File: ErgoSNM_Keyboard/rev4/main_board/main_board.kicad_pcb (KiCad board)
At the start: 2 copper layers, 116 parts, among them J1 Conn_MouseSensor, J2 Conn_CoreBoard, J3 Conn_MouseSensor, J4 Conn_Batt, J5 Conn_Batt, J6 Conn_CoreBoard, SW1 SW_DPDT_x2, SW2 RESET, SW3 RESET, SW4 SW_DPDT_x2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

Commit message: feat: update main board layout
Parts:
- removed C1, C2, C5, C6, C7, C8: 22uF, Capacitor_SMD:C_0805_2012Metric
- removed C10: 1uF, Capacitor_SMD:C_0603_1608Metric
- removed C11, C12: 4.7uF, Capacitor_SMD:C_0603_1608Metric
- removed C3, C4: 2.2uF, Capacitor_SMD:C_0603_1608Metric
- removed C9: 100nF, Capacitor_SMD:C_0603_1608Metric
- removed J4, J5: Conn_Batt, Connector_JST:JST_PH_S2B-PH-SM4-TB_1x02-1MP_P2.00mm_Horizontal
- removed L1: 1.5uH, Inductor_SMD:L_Changjiang_FNR252012S
- removed LD1, LD2: RED, LED_SMD:LED_0603_1608Metric
- removed R2: 1M, Resistor_SMD:R_0603_1608Metric
- removed R3: 180k, Resistor_SMD:R_0603_1608Metric
- removed R4, R5, R7: 10k, Resistor_SMD:R_0603_1608Metric
- removed R6: 2k, Resistor_SMD:R_0603_1608Metric
- removed SB1: Batt Switch Bypass, Jumper:SolderJumper-2_P1.3mm_Open_TrianglePad1.0x1.5mm
- removed SB2: Charger Select, Jumper:SolderJumper-3_P2.0mm_Open_TrianglePad1.0x1.5mm_NumberLabels
- removed SB3: Vsrc Select, Jumper:SolderJumper-3_P2.0mm_Open_TrianglePad1.0x1.5mm_NumberLabels
- removed SB4: Power Save, Jumper:SolderJumper-3_P2.0mm_Open_TrianglePad1.0x1.5mm_NumberLabels
- removed SB5: Charge Boost, Jumper:SolderJumper-2_P1.3mm_Open_TrianglePad1.0x1.5mm
- removed SW1, SW4: SW_DPDT_x2, ErgoSNM_Keyboard:MSKT-22D14-T
- removed TRRS1, TRRS2: PJ-393_TRRS_8P, ErgoSNM_Keyboard:PJ-393 8P TRRS
- removed U1: TPS63020, Package_SON:VSON-14-1EP_3x4.45mm_P0.65mm_EP1.6x4.2mm_ThermalVias
- removed U2: BQ24075RGT, Package_DFN_QFN:VQFN-16-1EP_3x3mm_P0.5mm_EP1.6x1.6mm
- H1, H2, H3, H4, H5, H6, R1: moved to B.Cu
- moved R1 148.6 mm to (96.0, 49.0), turned to -90 degrees
- moved J2 102.0 mm to (117.8, 46.4), turned to 0 degrees
- moved J6 102.0 mm to (117.8, 46.4), turned to 180 degrees
- moved SW2 4.79 mm to (101.5, 49.0)
- moved SW3 4.79 mm to (101.5, 49.0)
- moved J1 0.42 mm to (194.0, 133.1)
- moved J3 0.42 mm to (194.0, 133.1)
- turned H1 to 180 degrees
- turned H2 to 180 degrees
- turned H3 to 180 degrees
- turned H4 to 180 degrees
- turned H5 to 180 degrees
- turned H6 to 180 degrees
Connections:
- J2 pad 1: VBATT_{A} -> GND
- J2 pad 10: SCLK -> COL_1
- J2 pad 11: MOSI -> COL_0
- J2 pad 12: MISO -> ROW_4
- J2 pad 13: nCS -> ROW_3
- J2 pad 14: ROW_0 -> unconnected-(J2-Pin_14-Pad14)
- J2 pad 15: ROW_1 -> ROW_2
- J2 pad 16: ROW_2 -> ROW_1
- J2 pad 17: GND -> ROW_0
- J2 pad 18: ROW_3 -> nCS
- J2 pad 19: ROW_4 -> MISO
- J2 pad 2: VBUS -> unconnected-(J2-Pin_2-Pad2)
- J2 pad 20: COL_0 -> MOSI
- J2 pad 21: COL_1 -> SCLK
- J2 pad 22: COL_2 -> MOTION
- J2 pad 23: COL_3 -> unconnected-(J2-Pin_23-Pad23)
- J2 pad 24: COL_4 -> unconnected-(J2-Pin_24-Pad24)
- J2 pad 25: COL_5 -> GND
- J2 pad 26: GND -> RESET
- J2 pad 27: IO_0 -> VDD
- J2 pad 28: IO_1 -> VDD
- J2 pad 29: IO_2 -> unconnected-(J2-Pin_29-Pad29)
- J2 pad 3: VDD -> unconnected-(J2-Pin_3-Pad3)
- J2 pad 30: GND -> unconnected-(J2-Pin_30-Pad30)
- J2 pad 4: VDD -> IO_0
- J2 pad 5: RESET -> GND
- J2 pad 6: GND -> COL_5
- J2 pad 7: TX -> COL_4
- J2 pad 8: RX -> COL_3
- J2 pad 9: MOTION -> COL_2
- J6 pad 1: VBATT_{A} -> GND
- J6 pad 10: SCLK -> COL_1
- J6 pad 11: MOSI -> COL_0
- J6 pad 12: MISO -> ROW_4
- J6 pad 13: nCS -> ROW_3
- J6 pad 14: ROW_0 -> unconnected-(J6-Pin_14-Pad14)
- J6 pad 15: ROW_1 -> ROW_2
- J6 pad 16: ROW_2 -> ROW_1
- J6 pad 17: GND -> ROW_0
- J6 pad 18: ROW_3 -> nCS
- J6 pad 19: ROW_4 -> MISO
- J6 pad 2: VBUS -> unconnected-(J6-Pin_2-Pad2)
- J6 pad 20: COL_0 -> MOSI
- J6 pad 21: COL_1 -> SCLK
- J6 pad 22: COL_2 -> MOTION
- J6 pad 23: COL_3 -> unconnected-(J6-Pin_23-Pad23)
- J6 pad 24: COL_4 -> unconnected-(J6-Pin_24-Pad24)
- J6 pad 25: COL_5 -> GND
- J6 pad 26: GND -> RESET
- J6 pad 27: IO_0 -> VDD
- J6 pad 28: IO_1 -> VDD
- J6 pad 29: IO_2 -> unconnected-(J6-Pin_29-Pad29)
- J6 pad 3: VDD -> unconnected-(J6-Pin_3-Pad3)
- J6 pad 30: GND -> unconnected-(J6-Pin_30-Pad30)
- J6 pad 4: VDD -> IO_0
- J6 pad 5: RESET -> GND
- J6 pad 6: GND -> COL_5
- J6 pad 7: TX -> COL_4
- J6 pad 8: RX -> COL_3
- J6 pad 9: MOTION -> COL_2
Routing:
- net VDD: track 4.16 -> 242.8 mm, vias 0 -> 4
- net IO_0: track 4.16 -> 201.3 mm, vias 0 -> 3
- net nCS: track 4.16 -> 175.4 mm, vias 0 -> 2
- net MISO: track 4.16 -> 174.9 mm, vias 0 -> 2
- net MOTION: track 4.16 -> 174.1 mm, vias 0 -> 2
- net SCLK: track 4.16 -> 171.6 mm, vias 0 -> 2
- net MOSI: track 4.16 -> 169.0 mm, vias 0 -> 2
- net ROW_4: track 91.8 -> 200.7 mm, vias 0 -> 2
- net COL_5: track 90.7 -> 199.5 mm, vias 0 -> 4
- net ROW_3: track 110.4 -> 201.4 mm, vias 0 -> 2
- net COL_4: track 115.2 -> 203.3 mm, vias 0 -> 2
- net ROW_2: track 109.6 -> 179.3 mm, vias 0 -> 2
- net COL_3: track 115.2 -> 182.6 mm, vias 0 -> 2
- net RESET: track 0.00 -> 52.6 mm, vias 0 -> 4
- net ROW_1: track 111.7 -> 158.7 mm, vias 0 -> 2
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- added copper zone on B.Cu, net GND
- added copper zone on F.Cu, net GND
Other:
- board outline added: 117 x 107 mm

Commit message: feat: routed E73 core board
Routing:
- net COL_2: track 162.0 -> 158.8 mm
- net COL_3: track 182.6 -> 179.5 mm
- net COL_5: track 199.5 -> 196.4 mm
- net COL_4: track 203.3 -> 200.4 mm
- net GND: vias 53 -> 61
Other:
- board size 117 x 107 mm -> 116.6 x 107 mm
- board text added: "Early Supporter Edition"
- board text added: "ErgoSNM"
- board text added: "JLCJLCJLCJLC"
- board text added: "REV ${REVISION}"

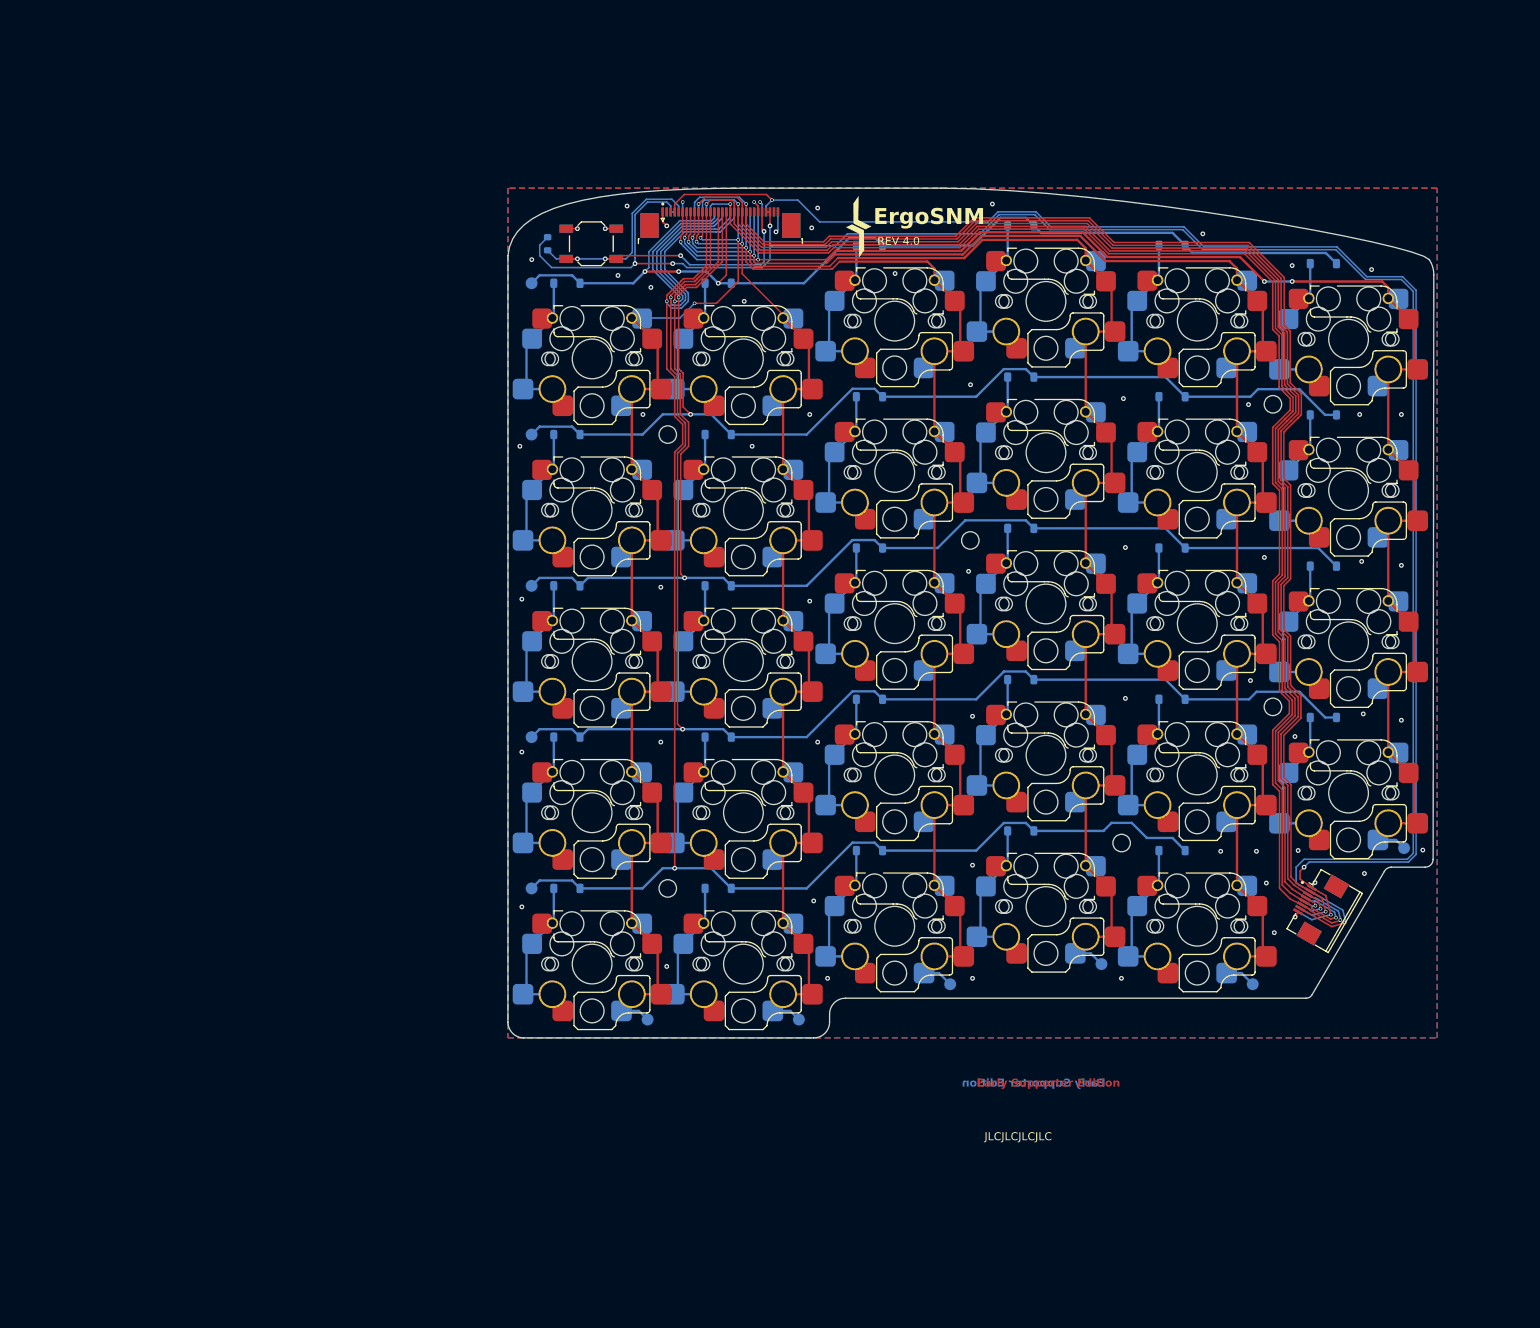
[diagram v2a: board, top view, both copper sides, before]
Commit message: feat: add 4x M2.5 mounting hole
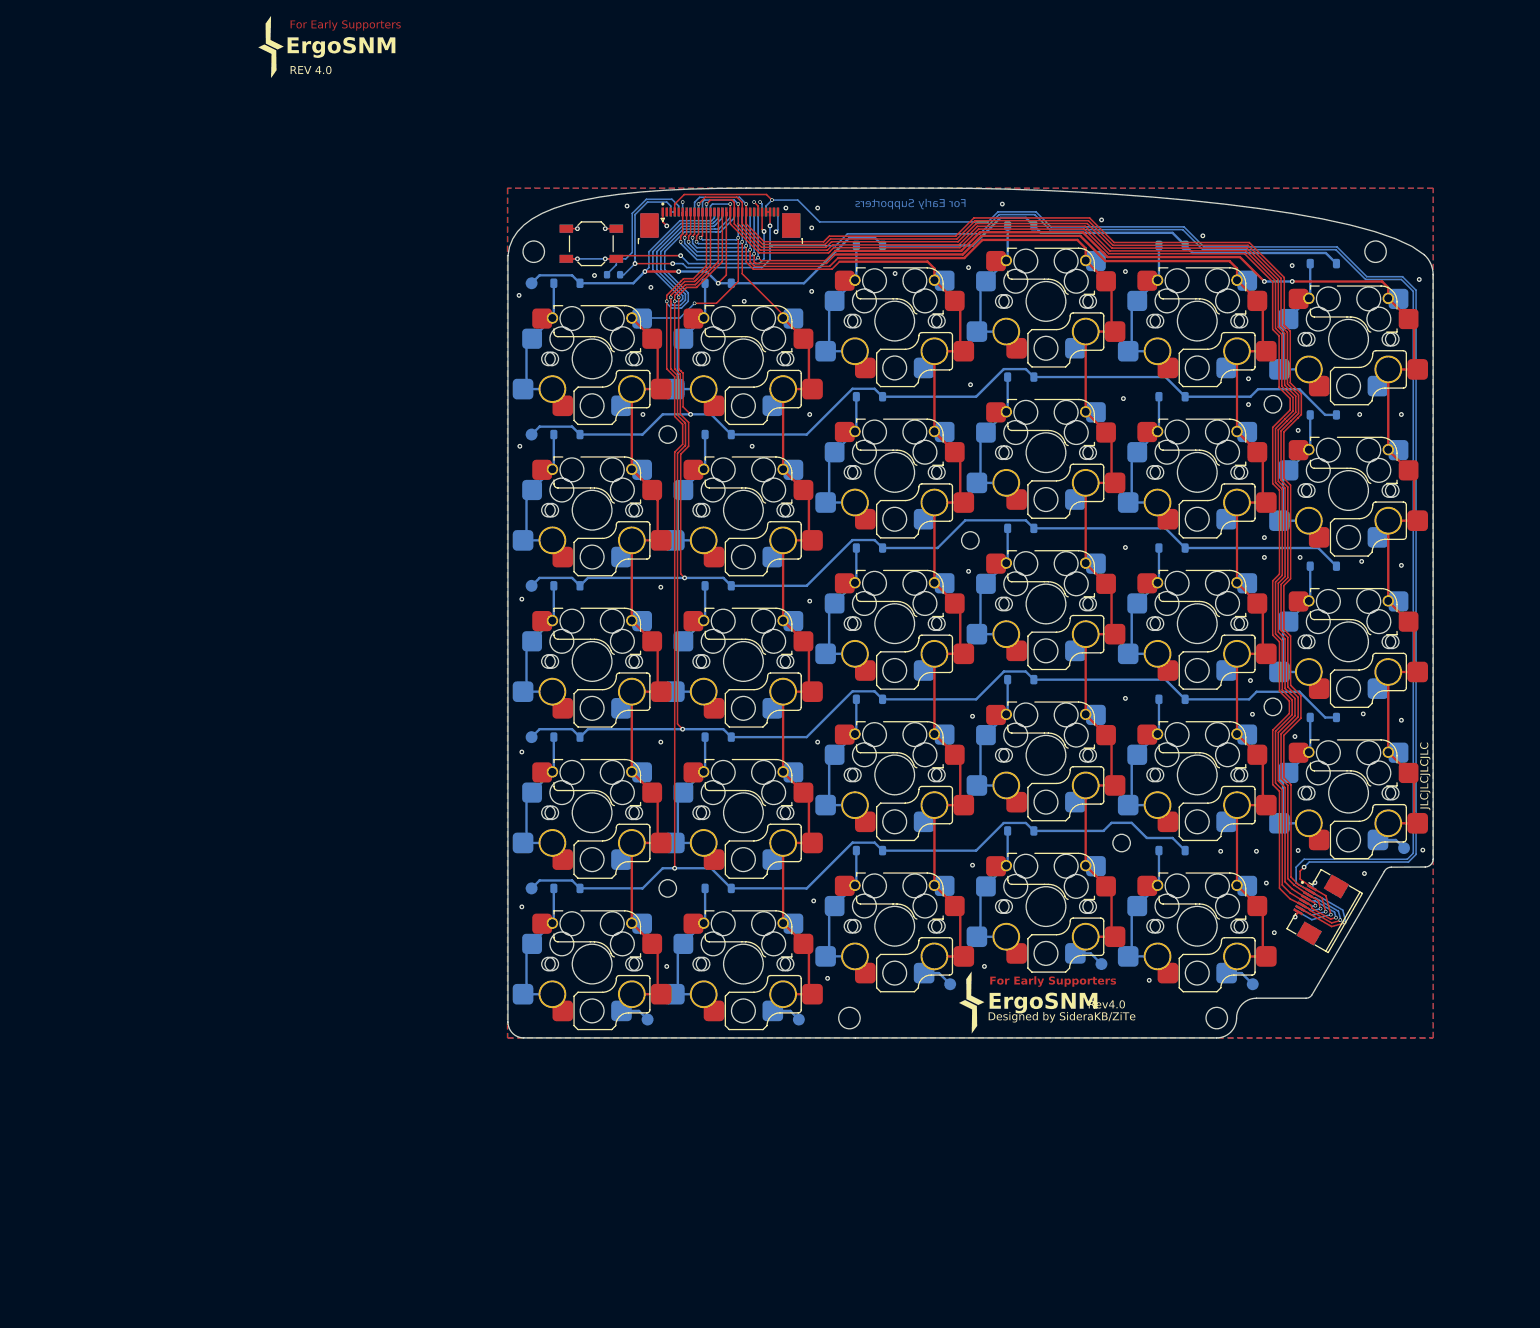
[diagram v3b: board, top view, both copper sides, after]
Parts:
- added H10: ~, MountingHole:MountingHole_2.7mm_M2.5_ISO14580, F.Cu at (180.2, 146.5)
- added H7: ~, MountingHole:MountingHole_2.7mm_M2.5_ISO14580, F.Cu at (94.2, 50.0)
- added H8: ~, MountingHole:MountingHole_2.7mm_M2.5_ISO14580, F.Cu at (200.2, 50.0)
- added H9: ~, MountingHole:MountingHole_2.7mm_M2.5_ISO14580, F.Cu at (134.0, 146.5)
- moved R1 9.17 mm to (104.3, 52.9), turned to 180 degrees
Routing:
- net VDD: track 242.8 -> 229.7 mm
- net RESET: track 52.6 -> 52.0 mm
- net GND: vias 61 -> 71
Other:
- board size 116.6 x 107 mm -> 116.5 x 107 mm
- board text added: "Designed by SideraKB/ZiTe"
- board text added: "For Early Supporters"
- board text added: "Rev${REVISION}"
- board text removed: "Early Supporter Edition"

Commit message: feat: update main board layout for 1.27mm pin header
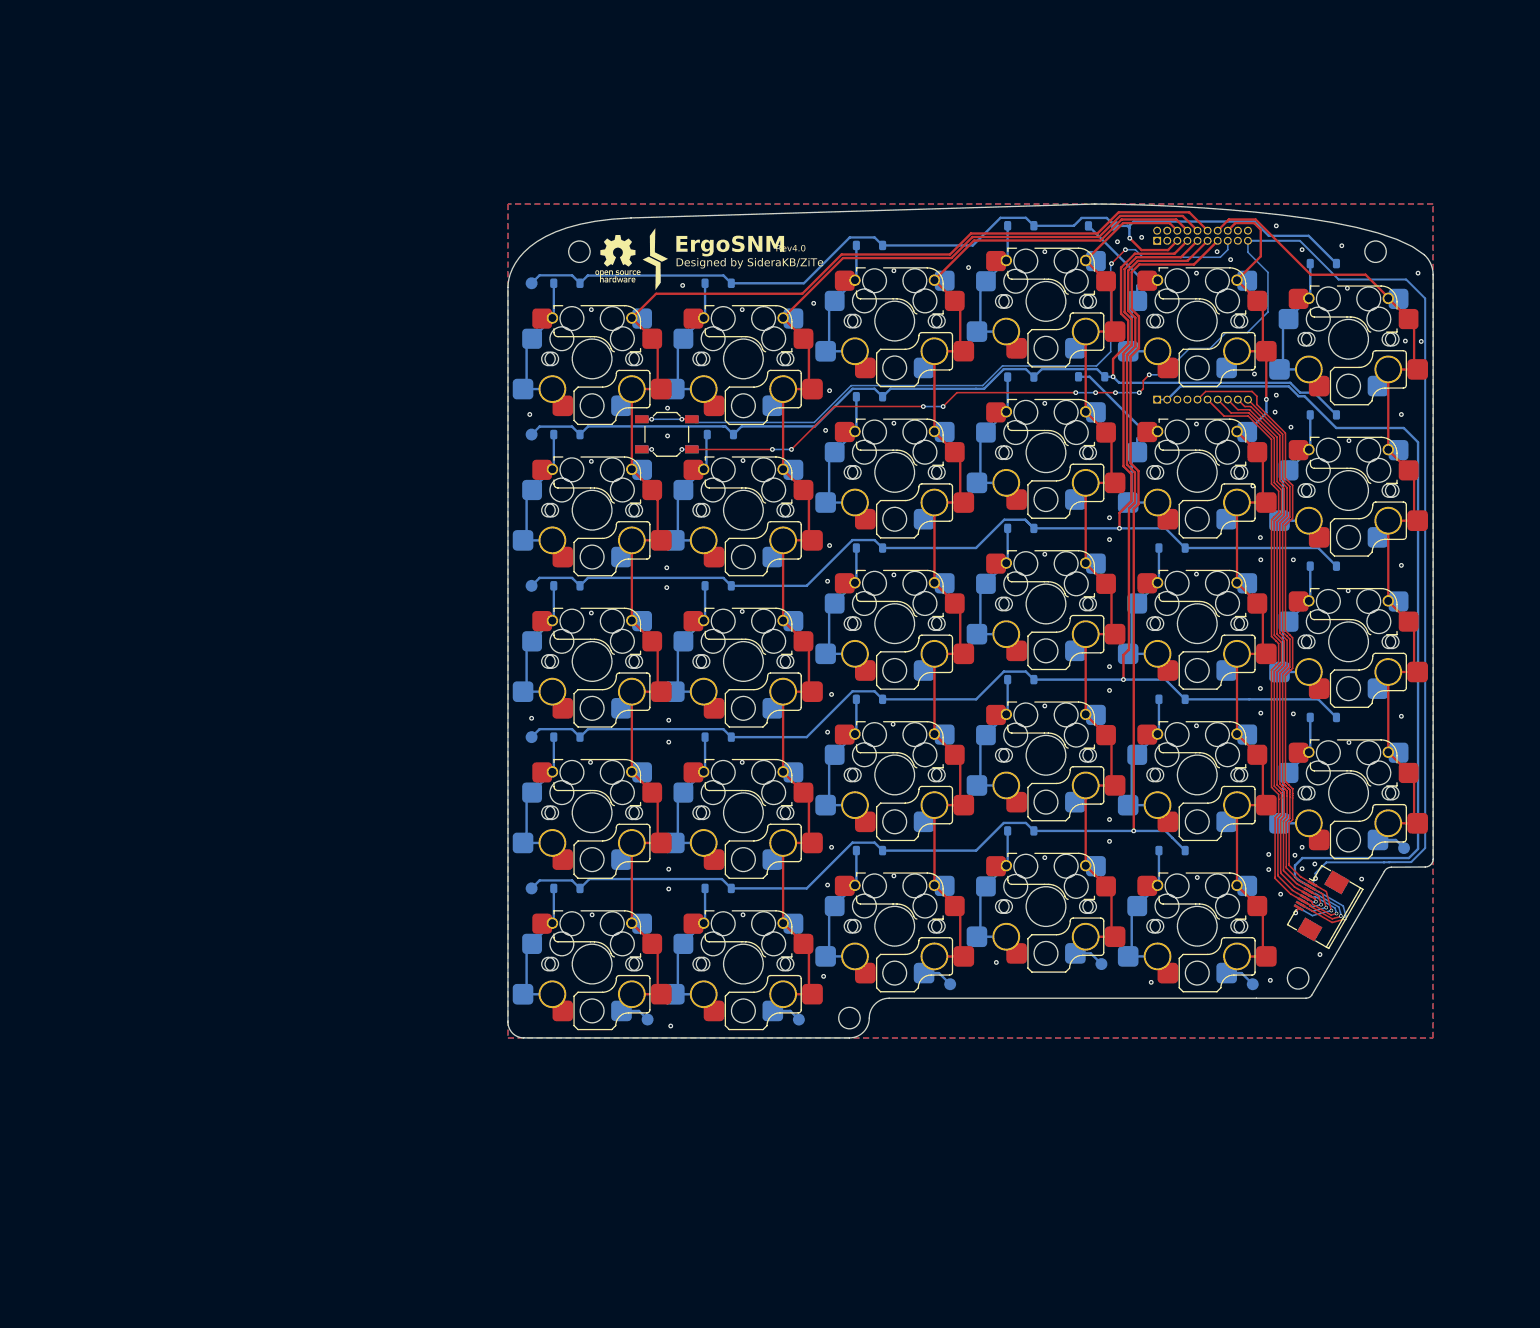
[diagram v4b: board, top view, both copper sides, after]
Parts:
- removed H1, H2, H3, H4, H5, H6: ~, MountingHole:MountingHole_2.2mm_M2_ISO7380
- removed J2, J6: Conn_CoreBoard, Connector_FFC-FPC:TE_3-1734839-0_1x30-1MP_P0.5mm_Horizontal
- removed R1: 10k, Resistor_SMD:R_0603_1608Metric
- added J4: Conn_01x10, Connector_PinSocket_1.27mm:PinSocket_1x10_P1.27mm_Vertical, B.Cu at (172.8, 68.6)
- added J5: Conn_02x10_Odd_Even, Connector_PinSocket_1.27mm:PinSocket_2x10_P1.27mm_Vertical, B.Cu at (172.8, 48.6)
- moved SW2 25.8 mm to (111.0, 73.0), turned to 180 degrees
- moved SW3 25.8 mm to (111.0, 73.0), turned to 0 degrees
- moved H10 11.4 mm to (190.5, 141.5)
- moved D11 10.4 mm to (164.5, 65.8)
- moved D5 9.21 mm to (165.8, 46.8)
- moved H7 5.75 mm to (100.0, 50.0)
- moved J1 0.52 mm to (194.0, 132.6)
- moved J3 0.52 mm to (194.0, 132.6)
- moved D8 0.28 mm to (117.8, 73.0)
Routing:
- net GND: track 12.9 -> 204.6 mm, vias 71 -> 107
- net IO_0: track 201.0 -> 83.5 mm, vias 3 -> 1
- net VDD: track 229.7 -> 120.5 mm, vias 4 -> 1
- net MOTION: track 174.1 -> 73.8 mm, vias 2 -> 1
- net SCLK: track 171.6 -> 73.2 mm, vias 2 -> 1
- net MOSI: track 169.0 -> 72.6 mm, vias 2 -> 1
- net MISO: track 174.9 -> 80.4 mm, vias 2 -> 1
- net nCS: track 175.4 -> 83.1 mm, vias 2 -> 1
- net COL_5: track 196.5 -> 117.0 mm, vias 4 -> 0
- net COL_4: track 200.5 -> 128.7 mm, vias 2 -> 1
- net COL_3: track 179.6 -> 129.0 mm, vias 2 -> 0
- net COL_0: track 147.4 -> 194.0 mm, vias 3 -> 0
- net RESET: track 52.0 -> 93.8 mm
- net COL_1: track 140.3 -> 173.3 mm, vias 2 -> 0
- net ROW_3: track 201.4 -> 174.5 mm, vias 2 -> 1
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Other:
- board size 116.5 x 107 mm -> 116.5 x 105 mm
- board text added: "Unit: mm"
- board text removed: "REV ${REVISION}"
